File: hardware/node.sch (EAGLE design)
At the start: 74 parts, among them IC1 MAX1555, IC2 TS5205, Q1 P-MOSFET, U1 ATMEGA32U4, U2 MCP1703CB/TOREX-XC6206, Y1 8MHz

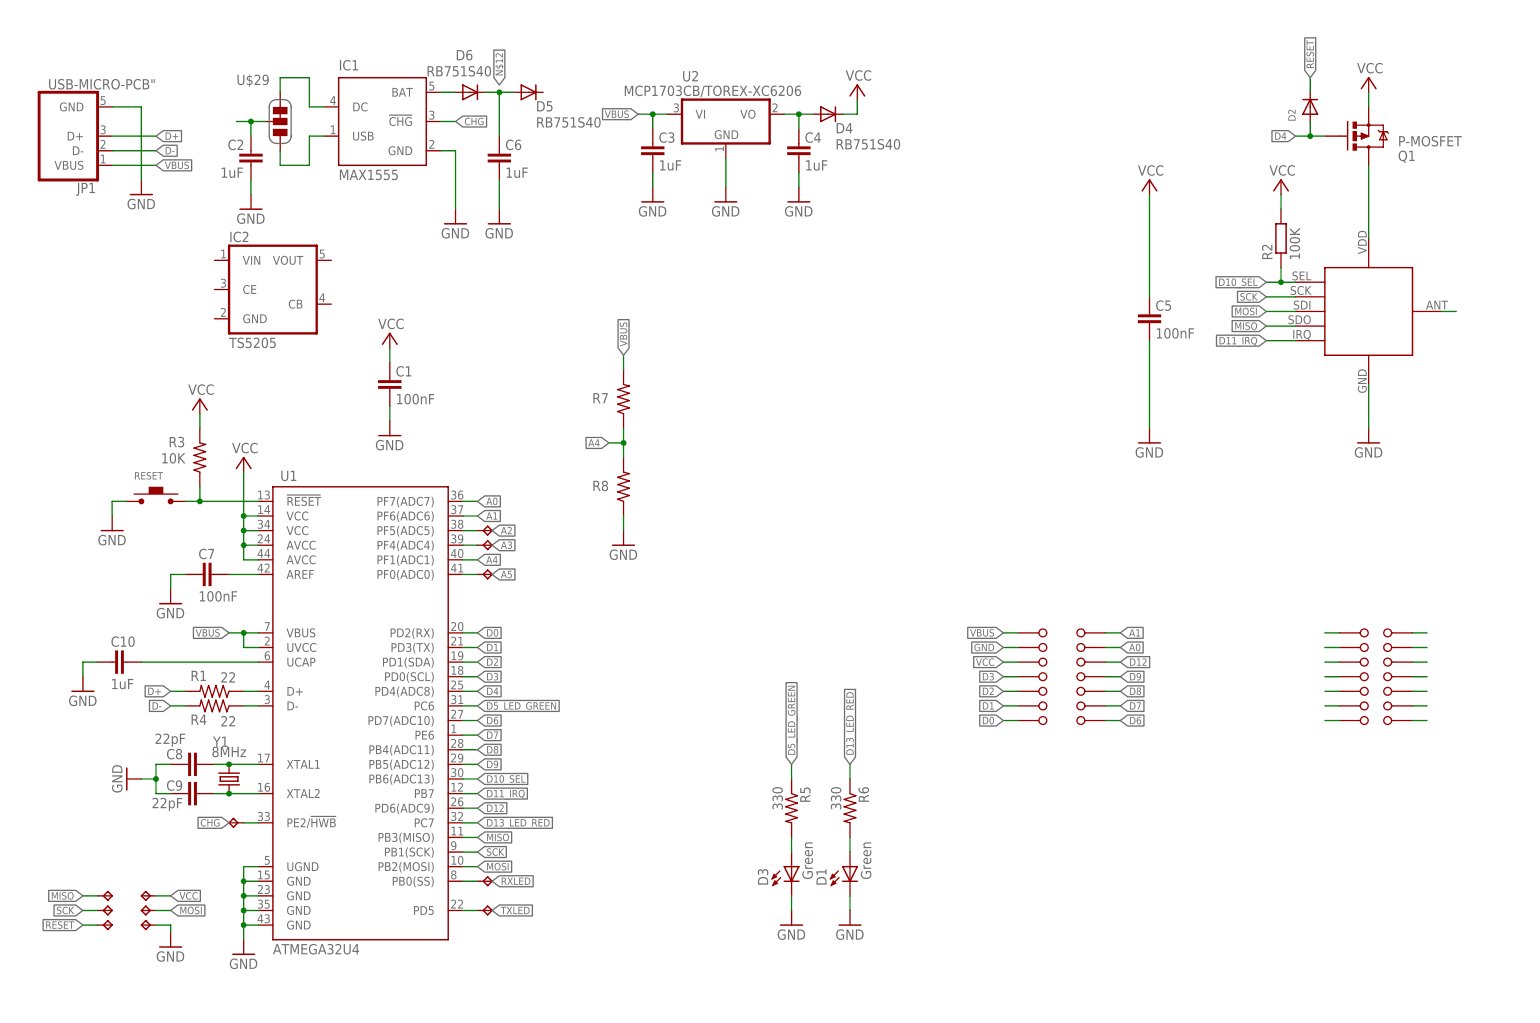
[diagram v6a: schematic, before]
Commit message: Node + Proto Shield + Lipo Shield
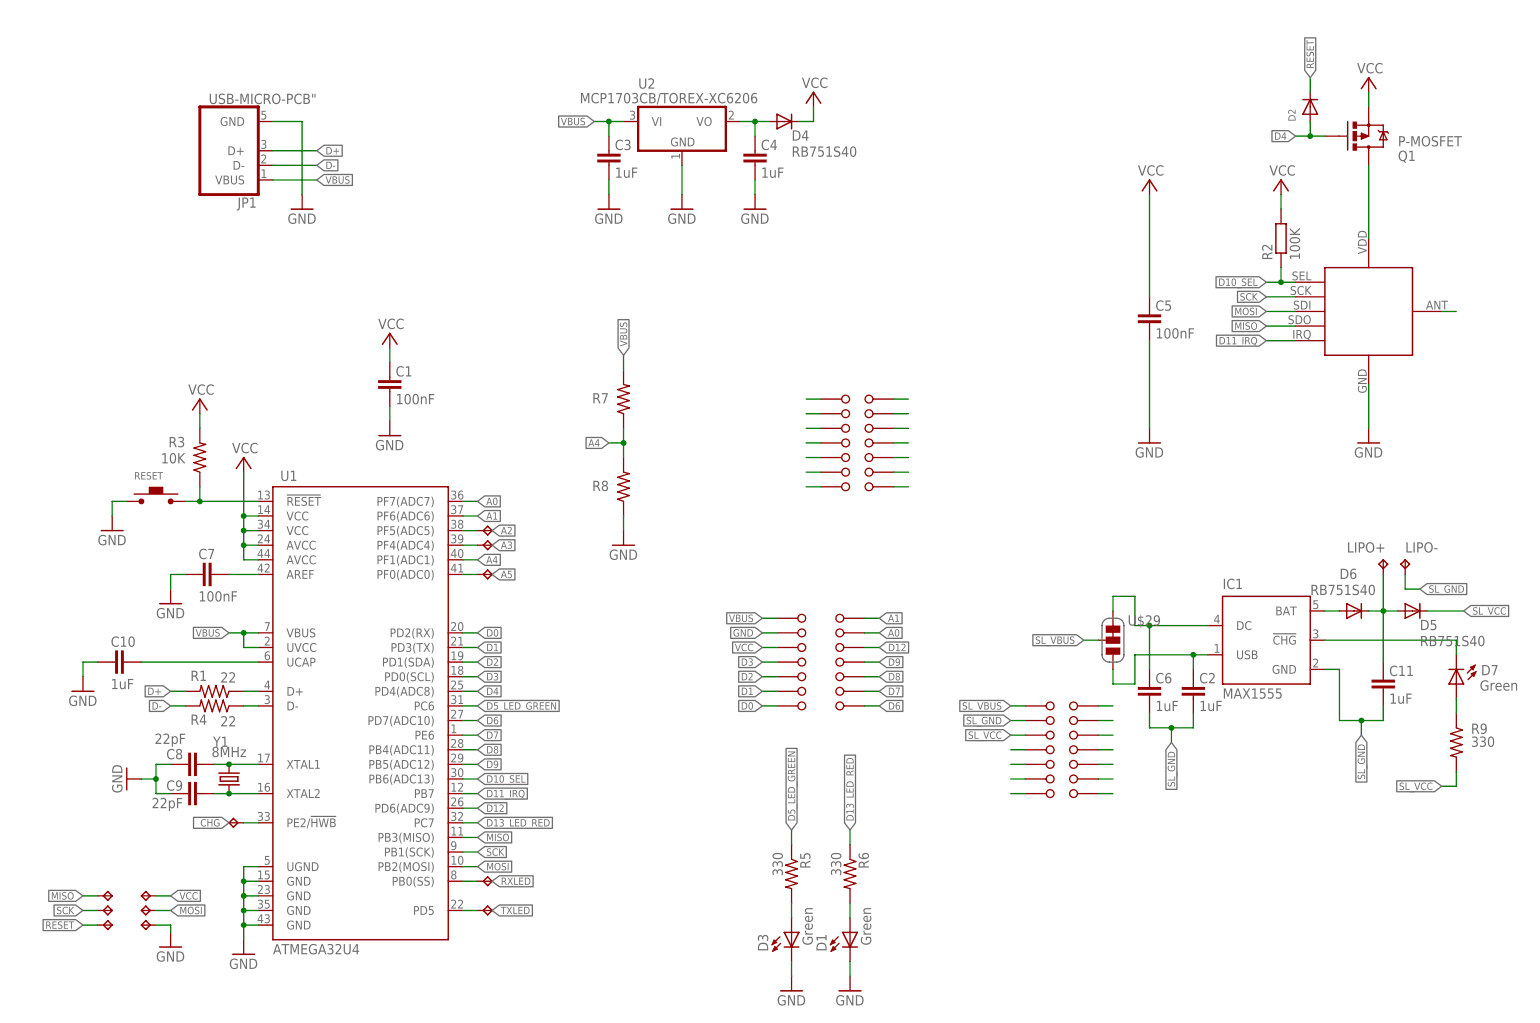
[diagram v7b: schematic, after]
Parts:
- removed IC2: TS5205, v-reg:TS5205
- added C11: 1uF, SparkFun:CAP0402-CAP
- added D7: Green, SparkFun:LED0603
- added LIPO+, LIPO-: TPPAD1-13, testpad:TPPAD1-13
- added R9: 330, SparkFun:RESISTOR0402-RES
- added U$30, U$31, U$32, U$33, U$34, U$35, U$36, U$37, U$38, U$39, U$40, U$41, U$42, U$43: IOPAD, openalarm:IOPAD
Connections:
- removed net CHG: IC1.!CHG, TP12.TP, U1.PE2/!HWB
- removed net N$12: C6.2, D5.A, D6.C
- removed net N$14: IC1.DC, U$29.C0
- removed net N$15: C2.2, U$29.COM
- new net N$133: D7.C, IC1.!CHG
- new net N$178: C6.2, IC1.DC, U$29.C0
- new net N$179: C2.2, IC1.USB, U$29.C1
- new net N$181: U$33.P$1
- new net N$182: U$34.P$1
- new net N$183: U$35.P$1
- new net N$184: U$36.P$1
- new net N$185: U$38.P$1
- new net N$186: U$39.P$1
- new net N$187: U$40.P$1
- new net N$188: U$41.P$1
- new net N$189: U$42.P$1
- new net N$190: U$43.P$1
- new net N$191: U$37.P$1
- new net N$192: C11.2, D5.A, D6.C, LIPO+.TP
- new net SL_GND: C11.1, C2.1, C6.1, IC1.GND, LIPO-.TP, U$31.P$1
- new net SL_VBUS: U$29.COM, U$30.P$1
- new net SL_VCC: D5.C, R9.2, U$32.P$1
- new net _CHG: TP12.TP, U1.PE2/!HWB
- net GND: no longer C2.1, C6.1, IC1.GND
- net N$11: now also D7.A, R9.1; no longer IC1.USB, U$29.C1
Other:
- note added: "LiPo Shield"
- note added: "Proto Shield"
- note removed: "Shield"
- moved on the sheet: C2, C3, C4, C6, D1, D3, D4, D5, D6, IC1, JP1, R5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

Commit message: Node + 2 Proto Shield + Lipo Shield
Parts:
- added U$44, U$45, U$46, U$47, U$48, U$49, U$50, U$51, U$52, U$53, U$54, U$55, U$56, U$57: IOPAD, openalarm:IOPAD
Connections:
- new net N$245: U$44.P$1
- new net N$246: U$45.P$1
- new net N$247: U$46.P$1
- new net N$248: U$47.P$1
- new net N$249: U$48.P$1
- new net N$250: U$49.P$1
- new net N$251: U$50.P$1
- new net N$252: U$52.P$1
- new net N$253: U$53.P$1
- new net N$254: U$54.P$1
- new net N$255: U$55.P$1
- new net N$256: U$56.P$1
- new net N$257: U$57.P$1
- new net N$258: U$51.P$1
